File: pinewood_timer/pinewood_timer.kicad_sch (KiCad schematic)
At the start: 11 parts, among them U1 STM32F091RCTx

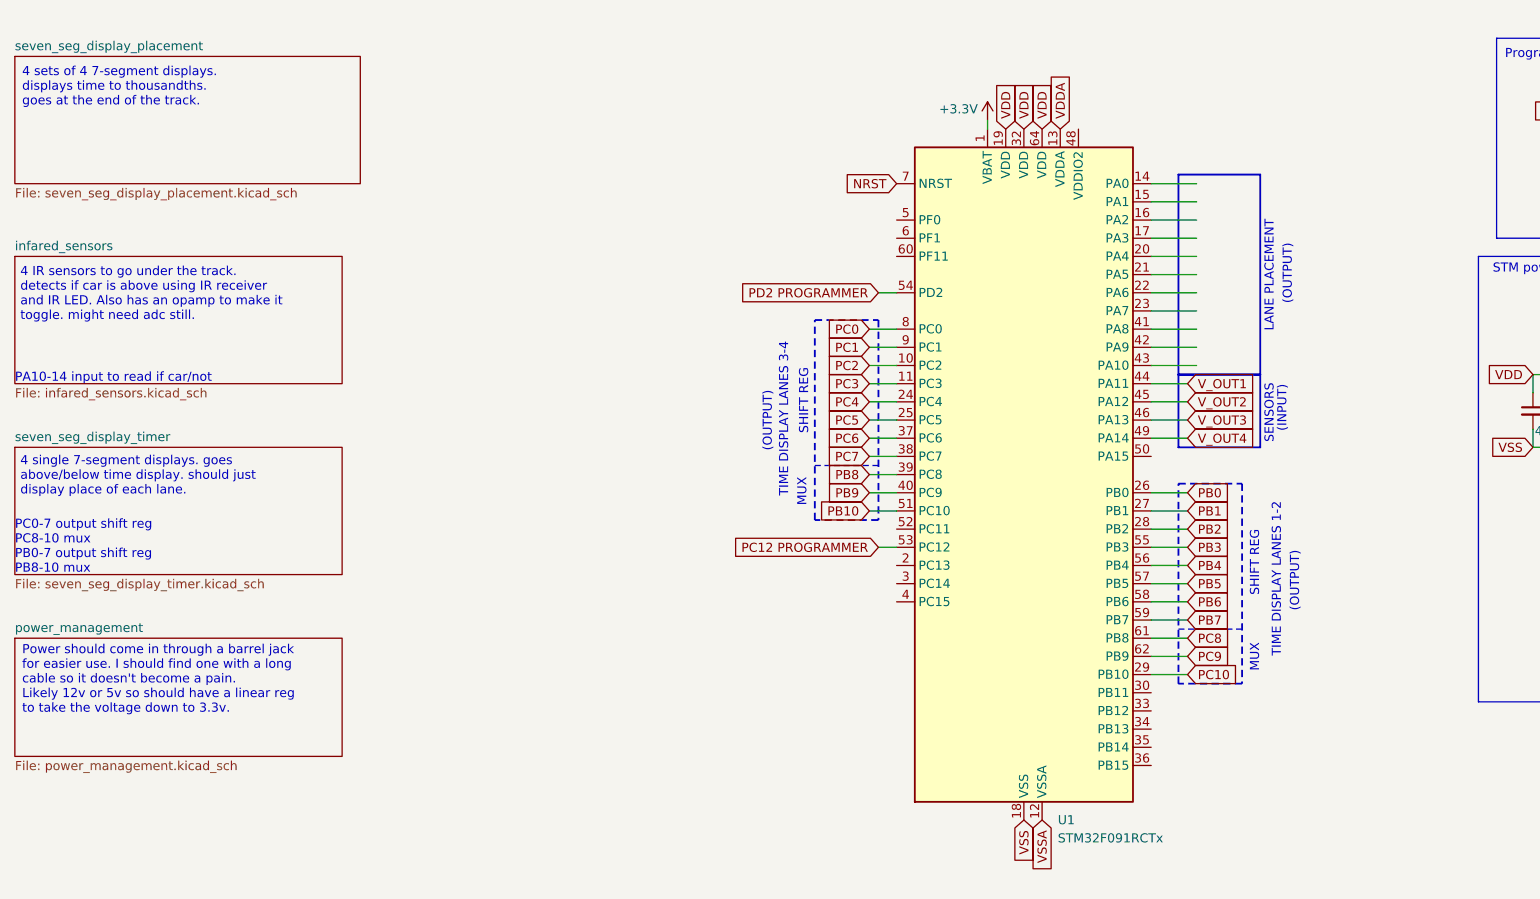
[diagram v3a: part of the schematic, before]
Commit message: worked on the ir sensors and placement display
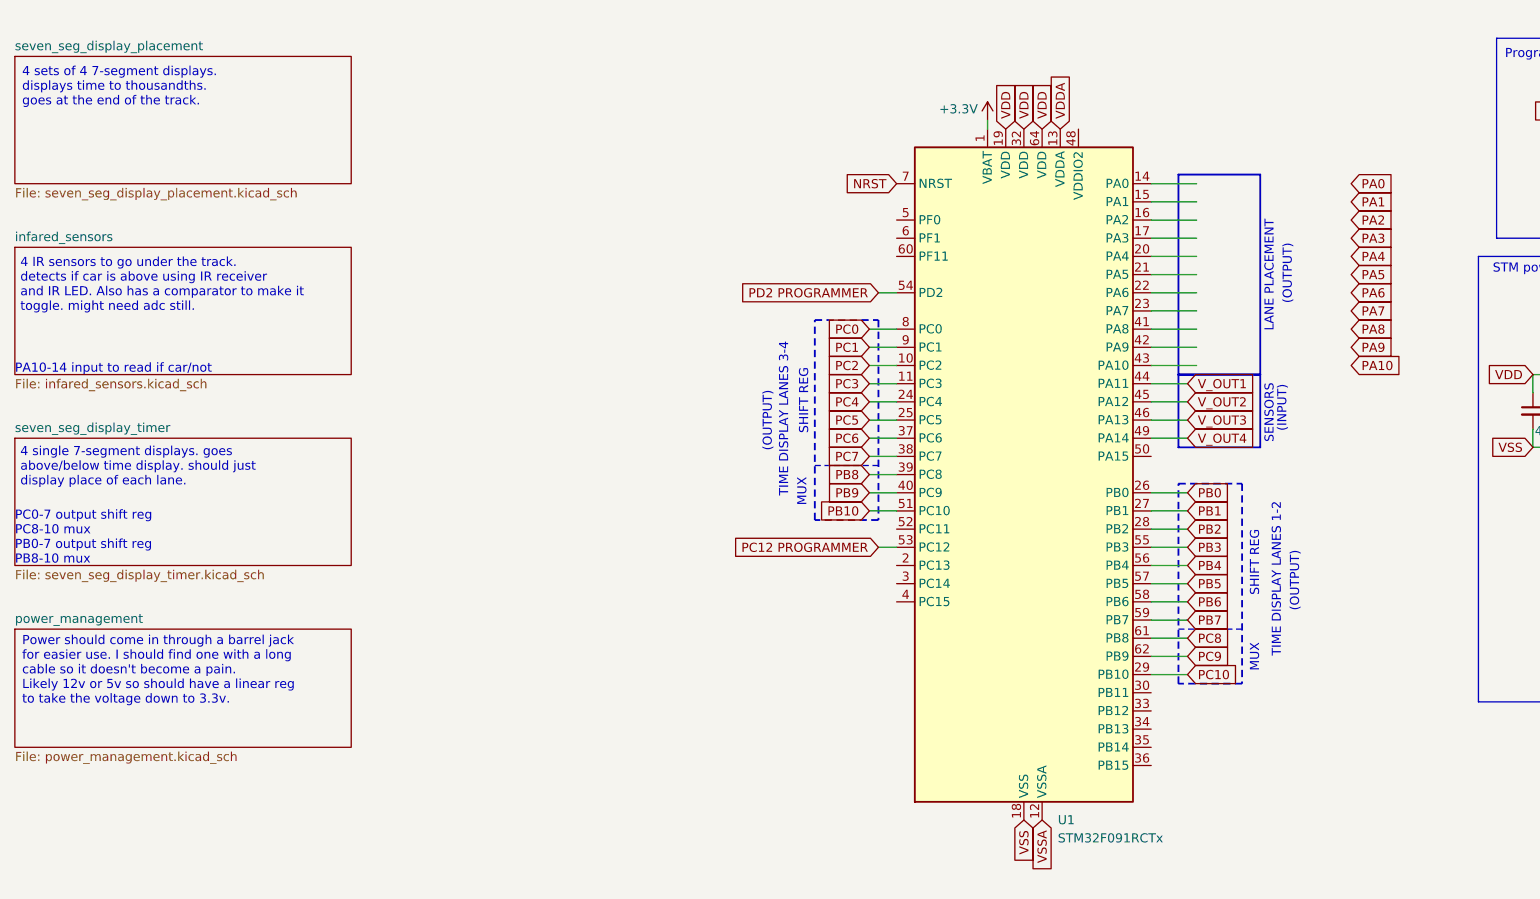
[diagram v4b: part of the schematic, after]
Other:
- note added: "4 IR sensors to go under the track. detects if car is above using IR receiver and IR LED. Also has a comparator to make it toggle. might need adc still."
- note removed: "4 IR sensors to go under the track. detects if car is above using IR receiver and IR LED. Also has an opamp to make it toggle. might need adc still."

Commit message: edited placement timer schematic since i can never make up my mind
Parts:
- added D5, D6, D7: LED, symbol Device:LED
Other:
- note added: "barrel jack 3.3v in only"
- note added: "i want to have a large reset button that is accessible to reset the track each run. i also want to have one on the board for funzies"
- note added: "status leds? *red - rebooting *green - ready *amber - timing?"
- note removed: "Power should come in through a barrel jack for easier use. I should find one with a long cable so it doesn't become a pain. Likely 12v or 5v so should have a linear reg to take the voltage down to 3.3v."
- moved on the sheet: C1, RST_Button1

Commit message: keep forgetting ot push - a lot of updates
fixed stm pinout. needs a lot more support than i was providing
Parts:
- removed C2: 4.7uF, Capacitor_SMD:C_0805_2012Metric_Pad1.18x1.45mm_HandSolder, symbol Device:C_Small
- removed C3, C4, C5, C6, C7: 100nF, Capacitor_SMD:C_0805_2012Metric_Pad1.18x1.45mm_HandSolder, symbol Device:C_Small
- removed C8: 1uF, Capacitor_SMD:C_0805_2012Metric_Pad1.18x1.45mm_HandSolder, symbol Device:C_Small
- removed PROGRAMMER1: PROGRAMMER, Connector_PinHeader_2.54mm:PinHeader_1x06_P2.54mm_Vertical, symbol Connector:Conn_01x06_Socket
- removed U1: STM32F091RCTx, Package_QFP:LQFP-64_10x10mm_P0.5mm, symbol MCU_ST_STM32F0:STM32F091RCTx
- added C10, C9: 22uF, symbol Device:C
- added C11, C14, C16, C17: 100nF, symbol Device:C
- added C12: 10uF, symbol Device:C
- added C13, C15: 10pF, symbol Device:C
- added C18: 10nF, symbol Device:C
- added C19, C20: 1uF, symbol Device:C
- added D8: RED, symbol Device:LED
- added FB1: 120R, symbol Device:FerriteBead
- added J1: Conn_01x18_Pin, symbol Connector:Conn_01x18_Pin
- added J4: Conn_01x11_Pin, symbol Connector:Conn_01x11_Pin
- added J5: Conn_01x04_Pin, symbol Connector:Conn_01x04_Pin
- added J6: USB_B_Micro, symbol Connector:USB_B_Micro
- added R41, R43: 1k5, symbol Device:R_US
- added R42: 10k, symbol Device:R_US
- added SW1: SW_SPDT, symbol Switch:SW_SPDT
- added U10: AMS1117-3.3, Package_TO_SOT_SMD:SOT-223-3_TabPin2, symbol Regulator_Linear:AMS1117-3.3
- added U11: STM32L151CBTxA, Package_QFP:LQFP-48_7x7mm_P0.5mm, symbol MCU_ST_STM32L1:STM32L151CBTxA
- added Y1: 16MHz, symbol Device:Crystal_GND24
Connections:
- net +3.3V: now also C10.1, C12.1, C14.1, C16.1, C17.1, C20.1, D8.2 (A), FB1.2, J1.2 (Pin_2), J5.1 (Pin_1), R43.1, SW1.3 (C), U10.2 (VO), U11.24 (VDD), U11.36 (VDD), U11.48 (VDD)
- net GND: now also C10.2, C11.2, C13.2, C15.2, C18.2, C19.2, C20.2, C9.2, J1.1 (Pin_1), J5.4 (Pin_4), J6.5 (GND), R41.1, SW1.1 (A), U10.1 (GND), U11.23 (VSS), U11.35 (VSS), U11.47 (VSS), U11.8 (VSSA), U11.9 (VDDA)
- net NRST: now also C11.1, U11.7 (NRST)
- new net: C12.2, C14.2, C16.2, C17.2
- new net: Y1.2, Y1.4
- new net: J4.1 (Pin_1), U11.10 (PA0)
- new net: J4.10 (Pin_10), U11.30 (PA9)
- new net: J4.11 (Pin_11), U11.31 (PA10)
- new net: J4.2 (Pin_2), U11.11 (PA1)
- new net: J4.3 (Pin_3), U11.12 (PA2)
- new net: J4.4 (Pin_4), U11.13 (PA3)
- new net: J4.5 (Pin_5), U11.14 (PA4)
- new net: J4.6 (Pin_6), U11.15 (PA5)
- new net: J4.7 (Pin_7), U11.16 (PA6)
- new net: J4.8 (Pin_8), U11.17 (PA7)
- new net: J4.9 (Pin_9), U11.29 (PA8)
- new net: J1.18 (Pin_18), U11.18 (PB0)
- new net: J1.17 (Pin_17), U11.19 (PB1)
- new net: J1.16 (Pin_16), U11.20 (PB2)
- new net: J1.8 (Pin_8), U11.21 (PB10)
- new net: J1.7 (Pin_7), U11.22 (PB11)
- new net: J1.6 (Pin_6), U11.25 (PB12)
- new net: J1.5 (Pin_5), U11.26 (PB13)
- new net: J1.4 (Pin_4), U11.27 (PB14)
- new net: J1.3 (Pin_3), U11.28 (PB15)
- new net: J1.15 (Pin_15), U11.39 (PB3)
- new net: J1.14 (Pin_14), U11.40 (PB4)
- new net: J1.13 (Pin_13), U11.41 (PB5)
- new net: J1.12 (Pin_12), U11.42 (PB6)
- new net: J1.11 (Pin_11), U11.43 (PB7)
- new net: J1.10 (Pin_10), U11.45 (PB8)
- new net: J1.9 (Pin_9), U11.46 (PB9)
- new net +3.3VA: C18.1, C19.1, FB1.1
- new net BOOT0: R42.2, U11.44 (BOOT0)
- new net HSE_IN: C13.1, U11.5 (PH0), Y1.1
- new net HSE_OUT: C15.1, U11.6 (PH1), Y1.3
- new net PWR_LED_CATHODE: D8.1 (K), R41.2
- new net SW_BOOT0: R42.1, SW1.2 (B)
- new net SW_CLK: J5.3 (Pin_3), U11.37 (PA14)
- new net SW_DIO: J5.2 (Pin_2), U11.34 (PA13)
- new net USB_D+: J6.3 (D+), R43.2, U11.33 (PA12)
- new net USB_D-: J6.2 (D-), U11.32 (PA11)
- new net VBUS: C9.1, J6.1 (VBUS), U10.3 (VI)
- no-connect marks 0 -> 7
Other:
- note added: "1x 100nF per VDD pin"
- note added: "USB App note AN4879"
- note added: "VDDA Filtering"
- note removed: "Programmer"
- note removed: "REQUIRED FOR THE STM"
- note removed: "STM power in decoupling caps"
